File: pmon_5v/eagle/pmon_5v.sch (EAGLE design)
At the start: 30 parts, among them J1 USB, J2 USB, J3 USB_A, J4 PINHD-2X3, Q1 16Mhz, U1 LTC2943, U2 FT232RL, U3 ATMEGA328TQFP32

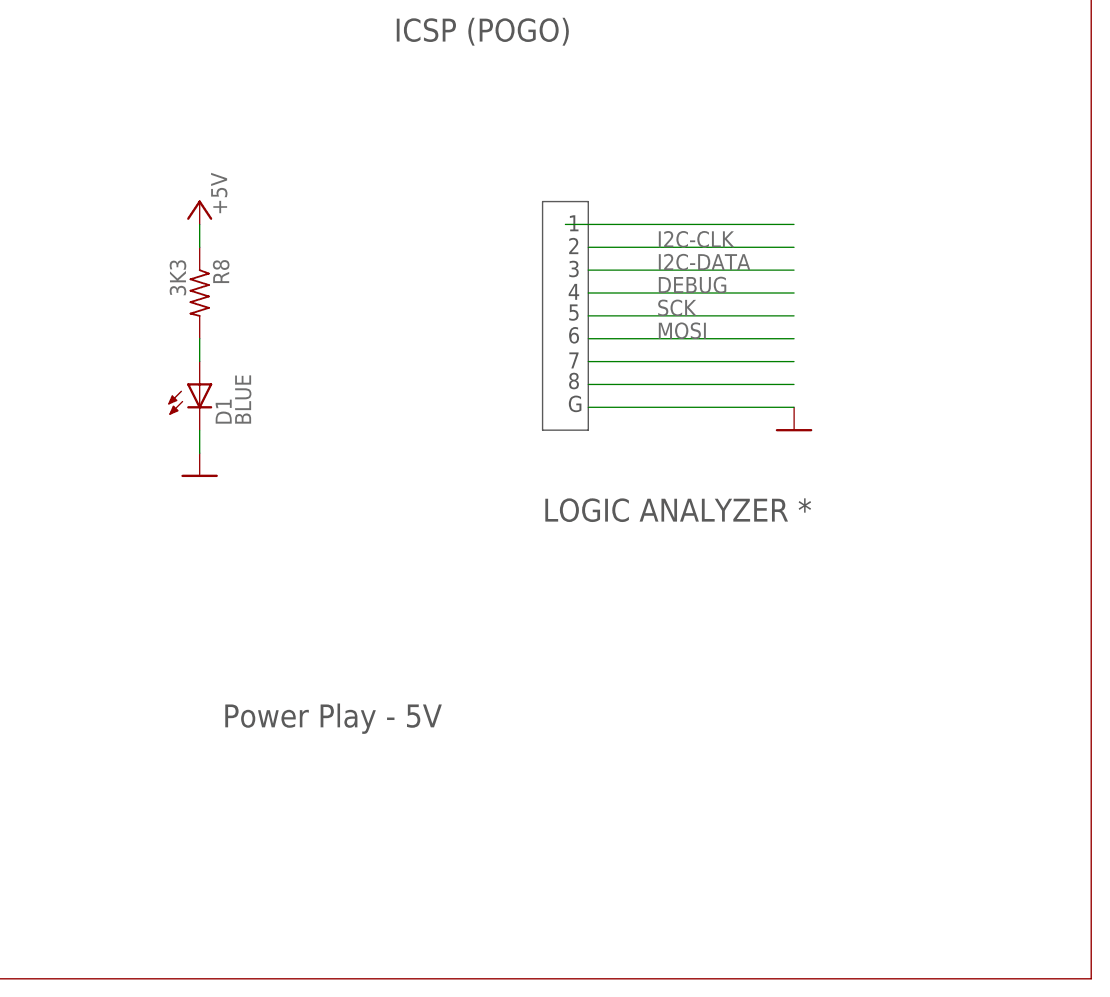
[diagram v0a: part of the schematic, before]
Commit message: Removed power led, added vias to the solder jumpers.
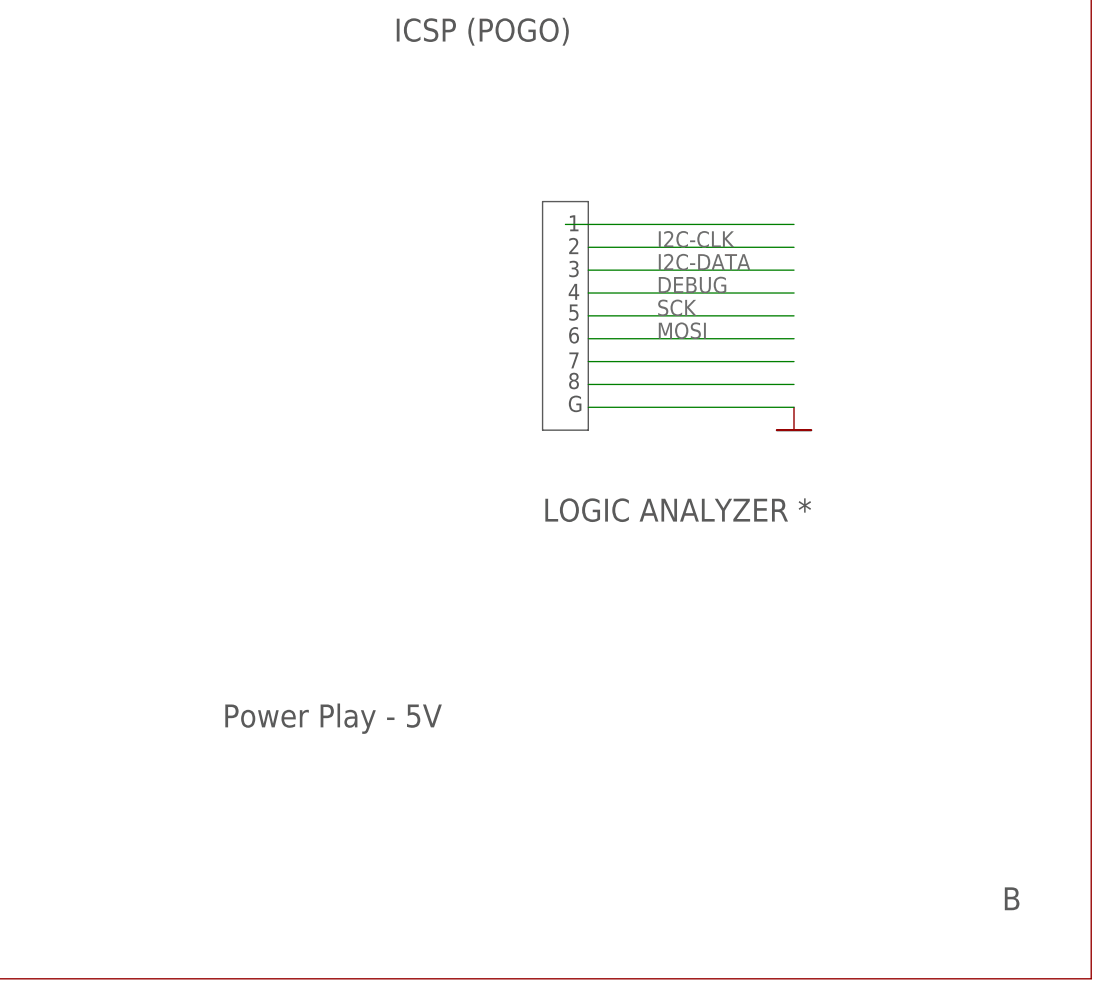
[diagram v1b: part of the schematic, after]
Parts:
- removed D1: BLUE, pmon_5v:LED1206
- removed R8: 3K3, pmon_5v:RES-R0603
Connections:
- removed net N$17: D1.A, R8.2
- net +5V: no longer R8.1
- net GND: no longer D1.C
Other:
- note added: "B"
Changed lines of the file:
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@@
 <part name="C2" library="pmon_5v" deviceset="CPOL-US" device="A/3216-18R" value="10uF"/>
 <part name="GND1" library="pmon_5v" deviceset="GND" device=""/>
-<part name="D1" library="pmon_5v" deviceset="LED" device="1206" value="BLUE"/>
-<part name="R8" library="pmon_5v" deviceset="RES-" device="R0603" value="3K3"/>
 <part name="C7" library="pmon_5v" deviceset="CAP-" device="C0603" value="0.1uF"/>
 <part name="C3" library="pmon_5v" deviceset="CAP-" device="C0603" value="0.1uF"/>
@@
 <part name="U$16" library="pmon_5v" deviceset="NC" device=""/>
 <part name="U$20" library="pmon_5v" deviceset="DOCFIELD" device=""/>
-<part name="GND18" library="pmon_5v" deviceset="GND" device=""/>
-<part name="P+3" library="pmon_5v" deviceset="+5V" device=""/>
 <part name="GND4" library="pmon_5v" deviceset="GND" device=""/>
 <part name="GND21" library="pmon_5v" deviceset="GND" device=""/>
@@
 <text x="165.1" y="152.4" size="2.54" layer="97">RESET*</text>
 <text x="78.994" y="57.404" size="2.032" layer="97">Dev</text>
+<text x="272.034" y="7.62" size="2.54" layer="97">B</text>
 </plain>
 <instances>
@@
 <instance part="C2" gate="G$1" x="12.7" y="48.26"/>
 <instance part="GND1" gate="1" x="170.18" y="208.28" rot="MR0"/>
-<instance part="D1" gate="G$1" x="182.88" y="66.04"/>
-<instance part="R8" gate="G$1" x="182.88" y="76.2" rot="R270"/>
 <instance part="C7" gate="G$1" x="68.58" y="40.64"/>
 <instance part="C3" gate="G$1" x="30.48" y="81.28" smashed="yes" rot="R270">
@@
 <instance part="U$16" gate="G$1" x="238.76" y="177.8" rot="R180"/>
 <instance part="U$20" gate="G$1" x="180.34" y="0"/>
-<instance part="GND18" gate="1" x="182.88" y="55.88" rot="MR0"/>
-<instance part="P+3" gate="1" x="182.88" y="86.36" smashed="yes">
-<attribute name="VALUE" x="185.928" y="84.836" size="1.778" layer="96" rot="R90"/>
-</instance>
 <instance part="GND4" gate="1" x="17.78" y="111.76"/>
 <instance part="GND21" gate="1" x="7.62" y="182.88"/>
@@
 <pinref part="U3" gate="G$1" pin="GND@1"/>
 <pinref part="U3" gate="G$1" pin="GND@2"/>
-</segment>
-<segment>
-<pinref part="D1" gate="G$1" pin="C"/>
-<pinref part="GND18" gate="1" pin="GND"/>
-<wire x1="182.88" y1="60.96" x2="182.88" y2="58.42" width="0.1524" layer="91"/>
 </segment>
 <segment>
@@
 <pinref part="U3" gate="G$1" pin="VCC@1"/>
 <pinref part="U3" gate="G$1" pin="VCC@2"/>
-</segment>
-<segment>
-<pinref part="R8" gate="G$1" pin="1"/>
-<wire x1="182.88" y1="83.82" x2="182.88" y2="81.28" width="0.1524" layer="91"/>
-<pinref part="P+3" gate="1" pin="+5V"/>
 </segment>
 <segment>
@@
 </segment>
 </net>
-<net name="N$17" class="0">
-<segment>
-<pinref part="D1" gate="G$1" pin="A"/>
-<pinref part="R8" gate="G$1" pin="2"/>
-<wire x1="182.88" y1="71.12" x2="182.88" y2="68.58" width="0.1524" layer="91"/>
-</segment>
-</net>

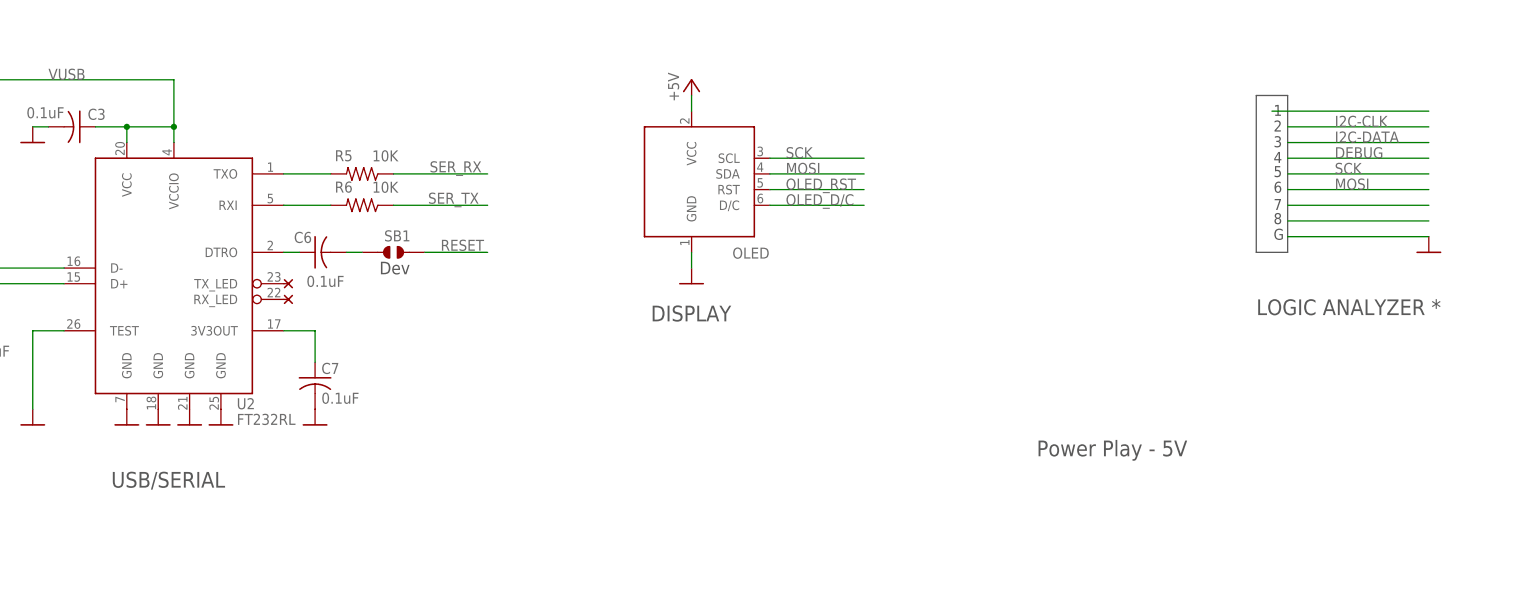
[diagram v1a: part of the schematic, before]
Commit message: Added pmon_5v BOM. Minor tweaks of schematics and layouts.
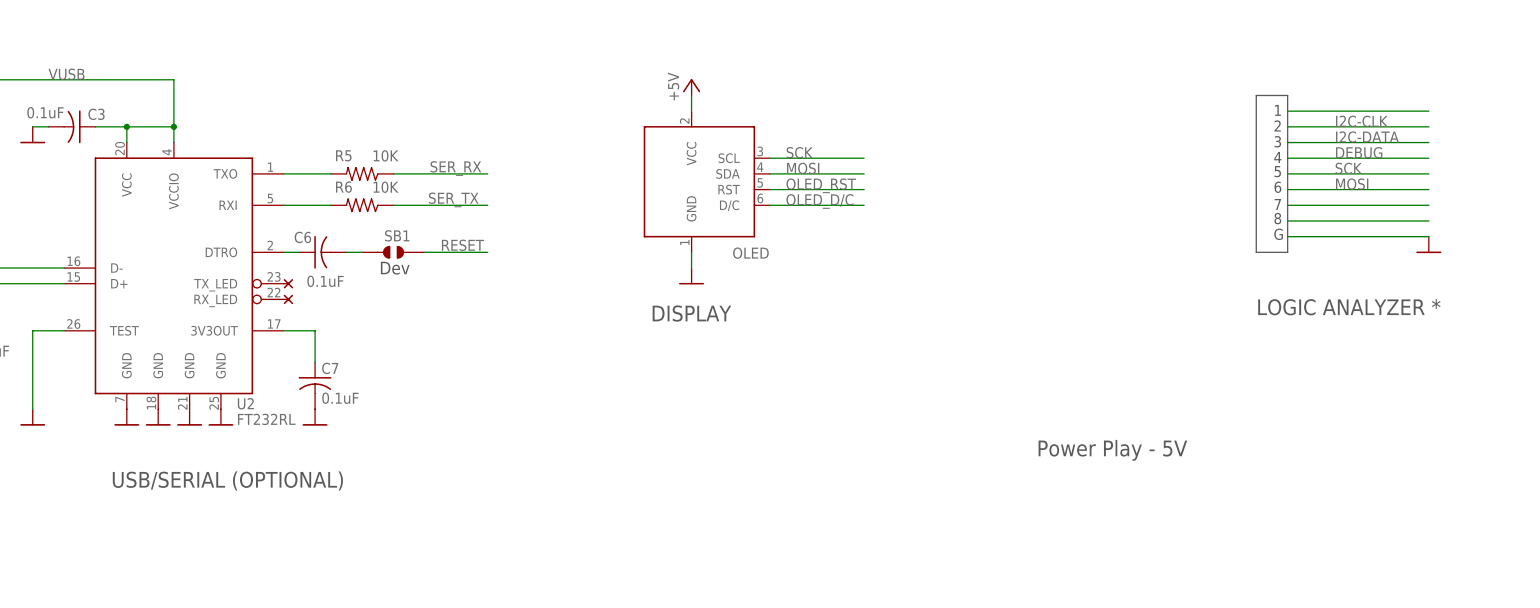
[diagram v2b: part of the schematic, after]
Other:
- note added: "USB/SERIAL (OPTIONAL)"
- note removed: "USB/SERIAL"
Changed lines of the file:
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@@
 <sheet>
 <plain>
-<text x="35.56" y="22.86" size="2.54" layer="97">USB/SERIAL</text>
+<text x="35.56" y="22.86" size="2.54" layer="97">USB/SERIAL (OPTIONAL)</text>
 <text x="204.47" y="104.14" size="2.54" layer="97">ICSP (POGO)</text>
 <text x="210.82" y="146.05" size="2.54" layer="97">MCU</text>
@@
 <net name="N$3" class="0">
 <segment>
-<wire x1="223.52" y1="83.82" x2="248.92" y2="83.82" width="0.1524" layer="91"/>
-</segment>
-</net>
+<wire x1="226.06" y1="83.82" x2="248.92" y2="83.82" width="0.1524" layer="91"/>
+</segment>
+</net>

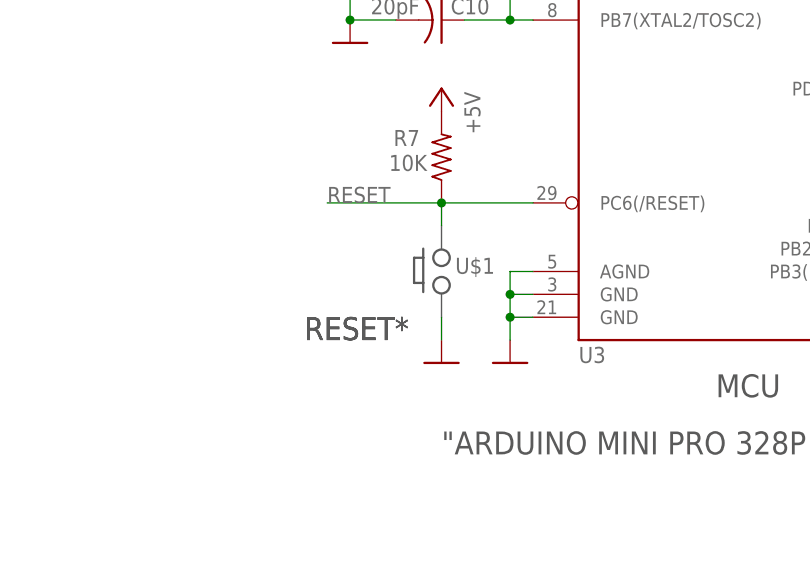
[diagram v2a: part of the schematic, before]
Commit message: Updated the LTC2943 footpting to match the datasheet (longer pads now).
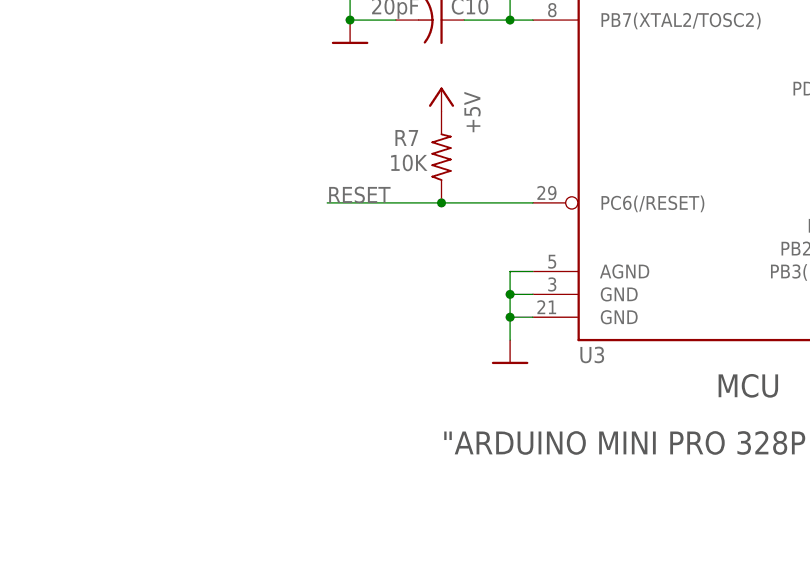
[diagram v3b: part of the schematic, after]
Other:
- note removed: "RESET*"
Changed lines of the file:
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@@
 <part name="U1" library="pmon_5v" deviceset="LTC2943" device="" value="LTC2943"/>
 <part name="GND17" library="pmon_5v" deviceset="GND" device=""/>
-<part name="GND31" library="pmon_5v" deviceset="GND" device=""/>
 <part name="R1" library="pmon_5v" deviceset="RES-" device="R0603" value="3K3"/>
 <part name="P+10" library="pmon_5v" deviceset="+5V" device=""/>
@@
 <part name="C9" library="pmon_5v" deviceset="CAP-" device="C0603" value="20pF"/>
 <part name="C10" library="pmon_5v" deviceset="CAP-" device="C0603" value="20pF"/>
-<part name="U$1" library="pmon_5v" deviceset="PUSH_BUTTON_GHOST" device=""/>
 <part name="U3" library="pmon_5v" deviceset="ATMEGA328" device="TQFP32"/>
 <part name="U2" library="pmon_5v" deviceset="FT232RL" device=""/>
@@
 <wire x1="220.98" y1="60.96" x2="220.98" y2="86.36" width="0.1524" layer="97"/>
 <text x="-25.4" y="7.62" size="2.54" layer="97">* PROTOTYPE ONLY</text>
-<text x="165.1" y="152.4" size="2.54" layer="97">RESET*</text>
 <text x="180.34" y="139.7" size="2.54" layer="97">"ARDUINO MINI PRO 328P 5V 16Mhz"</text>
 <text x="112.014" y="104.14" size="2.54" layer="97">ACTION</text>
 <text x="122.936" y="49.784" size="2.54" layer="97">DISPLAY</text>
-<text x="165.1" y="152.4" size="2.54" layer="97">RESET*</text>
 <text x="78.994" y="57.404" size="2.032" layer="97">Dev</text>
 <text x="272.034" y="7.62" size="2.54" layer="97">B</text>
@@
 <instance part="U1" gate="G$1" x="22.86" y="129.54"/>
 <instance part="GND17" gate="1" x="2.54" y="111.76"/>
-<instance part="GND31" gate="1" x="180.34" y="149.86"/>
 <instance part="R1" gate="G$1" x="43.18" y="137.16" smashed="yes" rot="R90">
 <attribute name="NAME" x="41.9354" y="131.826" size="1.778" layer="95" rot="R90"/>
@@
 <attribute name="VALUE" x="172.466" y="188.595" size="1.778" layer="96"/>
 </instance>
-<instance part="U$1" gate="G$1" x="180.34" y="160.02"/>
 <instance part="U3" gate="G$1" x="213.36" y="187.96"/>
 <instance part="U2" gate="1" x="45.72" y="53.34"/>
@@
 <wire x1="175.26" y1="187.96" x2="170.18" y2="187.96" width="0.1524" layer="91"/>
 <junction x="170.18" y="187.96"/>
-</segment>
-<segment>
-<pinref part="GND31" gate="1" pin="GND"/>
-<wire x1="180.34" y1="154.94" x2="180.34" y2="152.4" width="0.1524" layer="91"/>
 </segment>
 <segment>
@@
 <junction x="180.34" y="167.64"/>
 <label x="167.64" y="167.64" size="1.778" layer="95"/>
-<wire x1="180.34" y1="165.1" x2="180.34" y2="167.64" width="0.1524" layer="91"/>
 <pinref part="U3" gate="G$1" pin="PC6(/RESET)"/>
 </segment>
